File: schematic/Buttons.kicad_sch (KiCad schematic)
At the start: 6 parts, among them U5 GPTS203211B, U6 GPTS203211B, U7 GPTS203211B, U9 MAX6818EAP_T

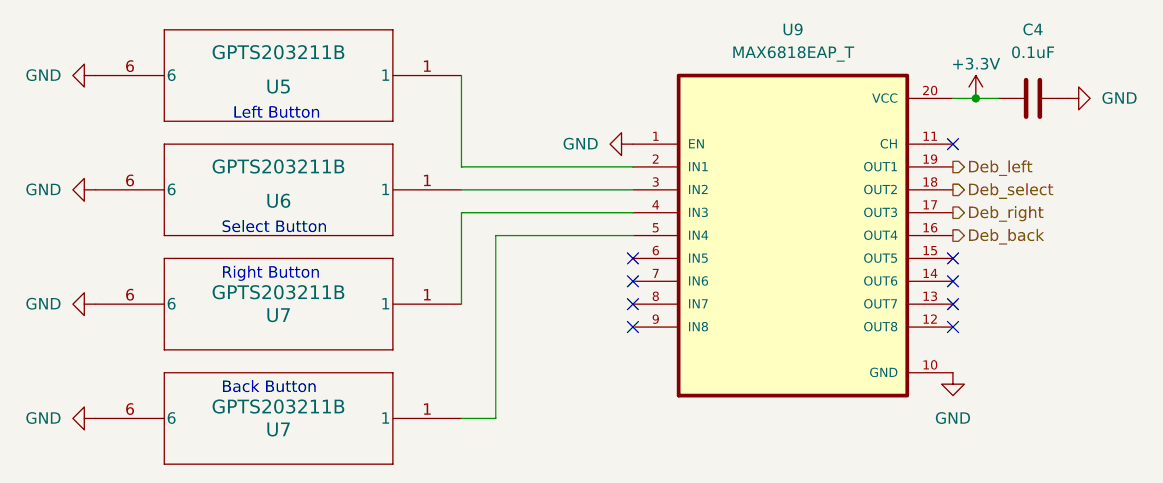
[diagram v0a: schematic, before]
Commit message: Changed to Kicad Version 8
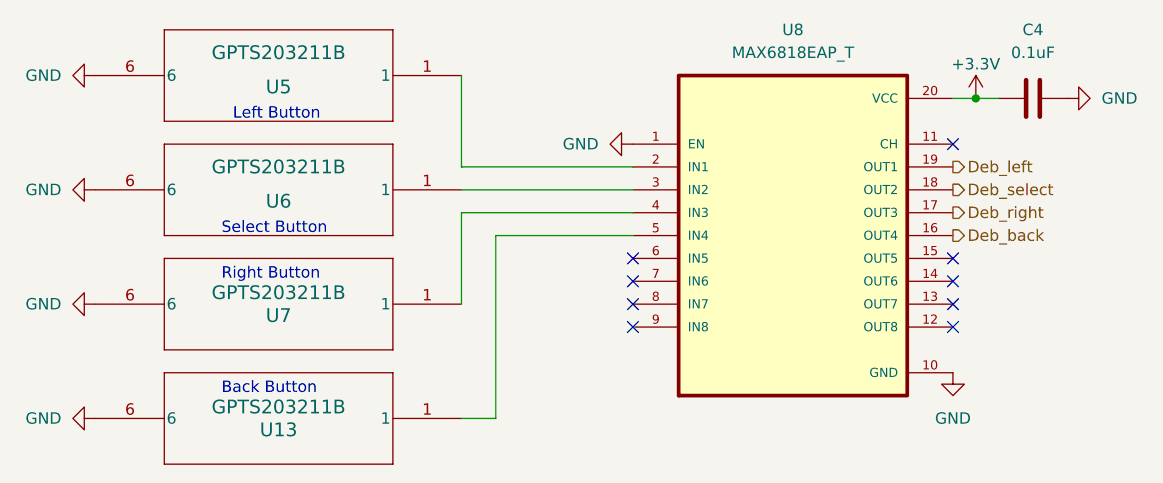
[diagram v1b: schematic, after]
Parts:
- renumbered U7 to U13, U9 to U8
